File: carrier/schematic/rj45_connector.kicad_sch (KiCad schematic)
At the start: 7 parts, among them J22001 KH-5224-8P8C-D

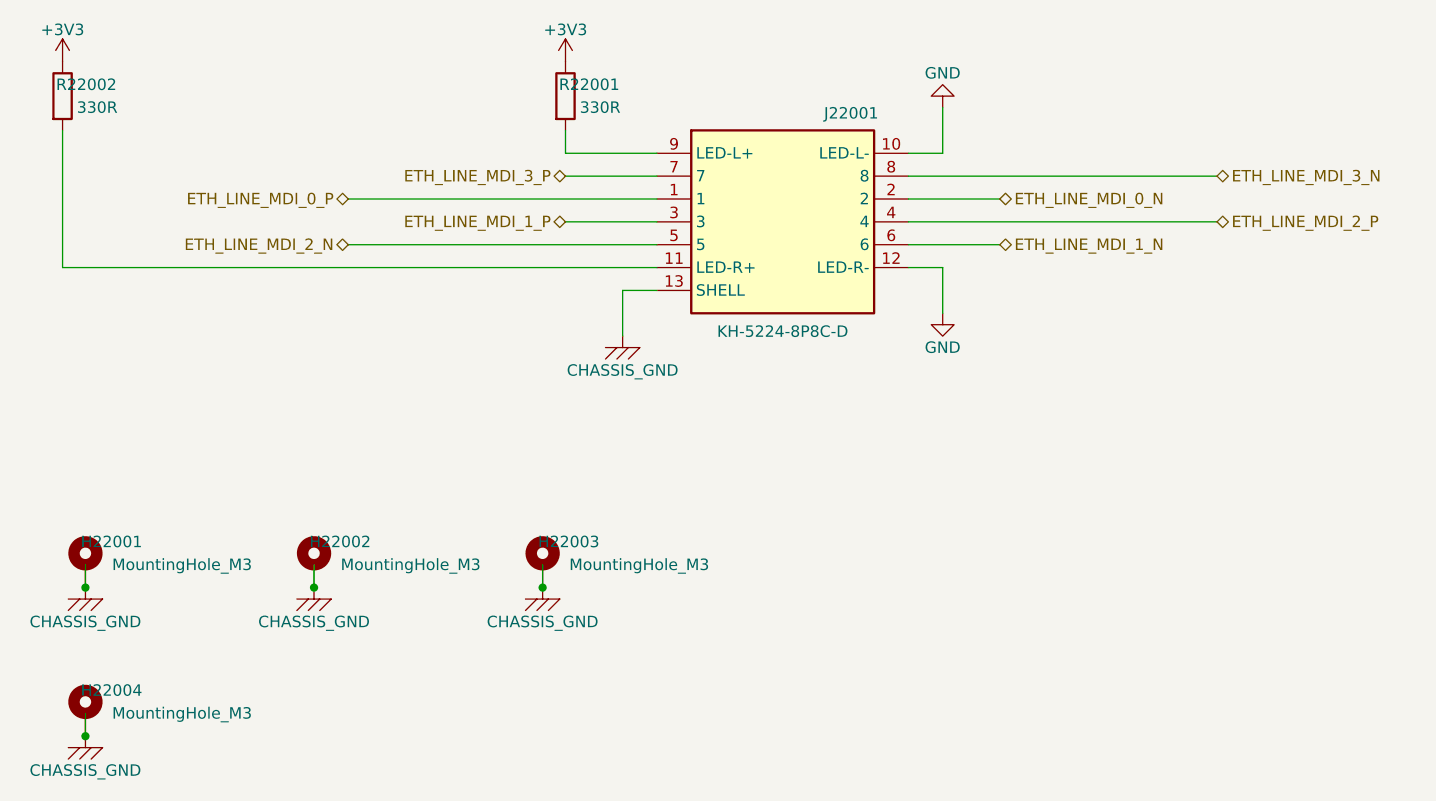
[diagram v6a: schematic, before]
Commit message: feat: USB-JTAG/UART debug bridge (CH347T) + Pmod expansion (Stream C)
Two new feature sheets (board 30 -> 33):
- usb_jtag + usb_jtag_connector: a self-powered, isolated USB-JTAG/UART debug
  bridge. CH347T (chosen over FT2232H, whose 64-pin LQFP the placer cannot route)
  on its own USB-powered island (AP2112K-3.3 LDO, USBLC6 ESD, 8MHz xtal); JTAG
  isolated to the Zynq via an SN74LVC125 buffer with default-Hi-Z OE (100k pull +
  DIP) so the existing debug_boot header owns JTAG by default (zero contention,
  netlist-proven: ZYNQ_JTAG touches only the buffer). Can program a dead board.
- pmod_expansion: a Digilent Pmod (2x6, 3.3V) — 8 IO on verified-free bank-13 PL
  pins (via FUNCTION_MAP) + a manually-gated rail + TPD4E1U06 ESD.

Pin alloc verified free (XDC 146 -> 156, no double-claims). Regression green:
board 33 sheets, selftest 59/59, pytest 219. usb_jtag render inspected (LAW 1).

Co-Authored-By: Claude Opus 4.8 <noreply@anthropic.com>
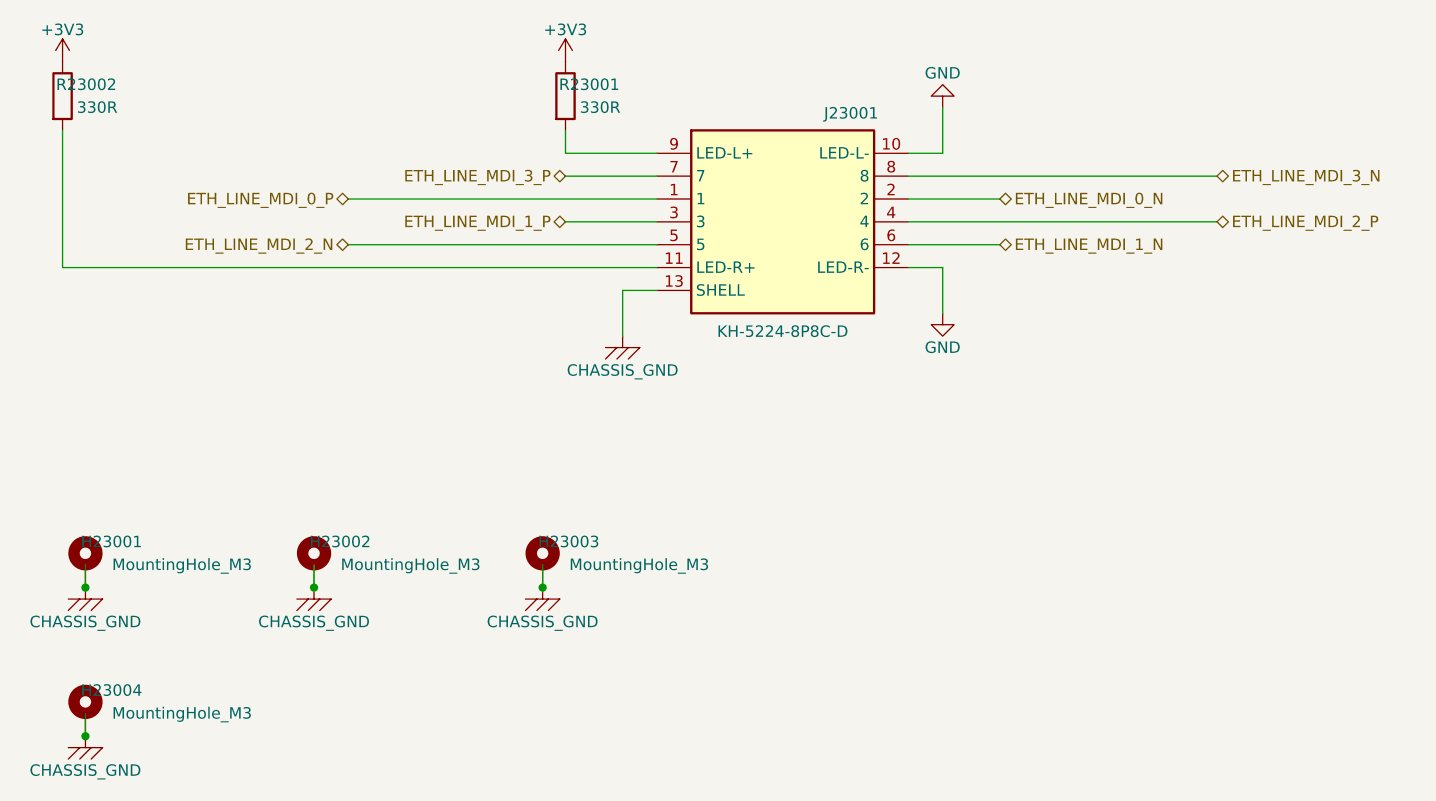
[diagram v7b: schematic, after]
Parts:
- renumbered H22001 to H23001, H22002 to H23002, H22003 to H23003, H22004 to H23004, J22001 to J23001, R22001 to R23001, R22002 to R23002
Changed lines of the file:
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@@
 		(property
 			"Reference"
-			"J22001"
+			"J23001"
 			(at 163.83 67.945 0)
 			(effects
@@
 				(path
 					"/c2797150-7a6e-556a-82f5-fdda13c31368/ae92c55a-3f4a-550a-b45e-435ced9eac9f"
-					(reference "J22001")
+					(reference "J23001")
 					(unit 1)
 				)
@@
 		(property
 			"Reference"
-			"R22001"
+			"R23001"
 			(at 134.722 64.77 0)
 			(effects
@@
 				(path
 					"/c2797150-7a6e-556a-82f5-fdda13c31368/ae92c55a-3f4a-550a-b45e-435ced9eac9f"
-					(reference "R22001")
+					(reference "R23001")
 					(unit 1)
 				)
@@
 		(property
 			"Reference"
-			"R22002"
+			"R23002"
 			(at 78.843 64.77 0)
 			(effects
@@
 				(path
 					"/c2797150-7a6e-556a-82f5-fdda13c31368/ae92c55a-3f4a-550a-b45e-435ced9eac9f"
-					(reference "R22002")
+					(reference "R23002")
 					(unit 1)
 				)
@@
 		(property
 			"Reference"
-			"H22001"
+			"H23001"
 			(at 81.637 115.57 0)
 			(effects
@@
 				(path
 					"/c2797150-7a6e-556a-82f5-fdda13c31368/ae92c55a-3f4a-550a-b45e-435ced9eac9f"
-					(reference "H22001")
+					(reference "H23001")
 					(unit 1)
 				)
@@
 		(property
 			"Reference"
-			"H22002"
+			"H23002"
 			(at 107.037 115.57 0)
 			(effects
@@
 				(path
 					"/c2797150-7a6e-556a-82f5-fdda13c31368/ae92c55a-3f4a-550a-b45e-435ced9eac9f"
-					(reference "H22002")
+					(reference "H23002")
 					(unit 1)
 				)
@@
 		(property
 			"Reference"
-			"H22003"
+			"H23003"
 			(at 132.437 115.57 0)
 			(effects
@@
 				(path
 					"/c2797150-7a6e-556a-82f5-fdda13c31368/ae92c55a-3f4a-550a-b45e-435ced9eac9f"
-					(reference "H22003")
+					(reference "H23003")
 					(unit 1)
 				)
@@
 		(property
 			"Reference"
-			"H22004"
+			"H23004"
 			(at 81.637 132.08 0)
 			(effects
@@
 				(path
 					"/c2797150-7a6e-556a-82f5-fdda13c31368/ae92c55a-3f4a-550a-b45e-435ced9eac9f"
-					(reference "H22004")
+					(reference "H23004")
 					(unit 1)
 				)
@@
 		(property
 			"Reference"
-			"#PWR22001"
+			"#PWR23001"
 			(at 138.43 90.17 0)
 			(effects
@@
 				(path
 					"/c2797150-7a6e-556a-82f5-fdda13c31368/ae92c55a-3f4a-550a-b45e-435ced9eac9f"
-					(reference "#PWR22001")
+					(reference "#PWR23001")
 					(unit 1)
 				)
@@
 		(property
 			"Reference"
-			"#PWR22002"
+			"#PWR23002"
 			(at 132.08 59.69 0)
 			(effects
@@
 				(path
 					"/c2797150-7a6e-556a-82f5-fdda13c31368/ae92c55a-3f4a-550a-b45e-435ced9eac9f"
-					(reference "#PWR22002")
+					(reference "#PWR23002")
 					(unit 1)
 				)
@@
 		(property
 			"Reference"
-			"#PWR22003"
+			"#PWR23003"
 			(at 76.2 59.69 0)
 			(effects
@@
 				(path
 					"/c2797150-7a6e-556a-82f5-fdda13c31368/ae92c55a-3f4a-550a-b45e-435ced9eac9f"
-					(reference "#PWR22003")
+					(reference "#PWR23003")
 					(unit 1)
 				)
@@
 		(property
 			"Reference"
-			"#PWR22004"
+			"#PWR23004"
 			(at 173.99 64.77 0)
 			(effects
@@
 				(path
 					"/c2797150-7a6e-556a-82f5-fdda13c31368/ae92c55a-3f4a-550a-b45e-435ced9eac9f"
-					(reference "#PWR22004")
+					(reference "#PWR23004")
 					(unit 1)
 				)
@@
 		(property
 			"Reference"
-			"#PWR22005"
+			"#PWR23005"
 			(at 173.99 87.63 0)
 			(effects
@@
 				(path
 					"/c2797150-7a6e-556a-82f5-fdda13c31368/ae92c55a-3f4a-550a-b45e-435ced9eac9f"
-					(reference "#PWR22005")
+					(reference "#PWR23005")
 					(unit 1)
 				)
@@
 		(property
 			"Reference"
-			"#PWR22009"
+			"#PWR23009"
 			(at 78.74 118.11 0)
 			(effects
@@
 				(path
 					"/c2797150-7a6e-556a-82f5-fdda13c31368/ae92c55a-3f4a-550a-b45e-435ced9eac9f"
-					(reference "#PWR22009")
+					(reference "#PWR23009")
 					(unit 1)
 				)
@@
 		(property
 			"Reference"
-			"#PWR22010"
+			"#PWR23010"
 			(at 104.14 118.11 0)
 			(effects
@@
 				(path
 					"/c2797150-7a6e-556a-82f5-fdda13c31368/ae92c55a-3f4a-550a-b45e-435ced9eac9f"
-					(reference "#PWR22010")
+					(reference "#PWR23010")
 					(unit 1)
 				)
@@
 		(property
 			"Reference"
-			"#PWR22011"
+			"#PWR23011"
 			(at 129.54 118.11 0)
 			(effects
@@
 				(path
 					"/c2797150-7a6e-556a-82f5-fdda13c31368/ae92c55a-3f4a-550a-b45e-435ced9eac9f"
-					(reference "#PWR22011")
+					(reference "#PWR23011")
 					(unit 1)
 				)
@@
 		(property
 			"Reference"
-			"#PWR22012"
+			"#PWR23012"
 			(at 78.74 134.62 0)
 			(effects
@@
 				(path
 					"/c2797150-7a6e-556a-82f5-fdda13c31368/ae92c55a-3f4a-550a-b45e-435ced9eac9f"
-					(reference "#PWR22012")
-					(unit 1)
-				)
+					(reference "#PWR23012")
+					(unit 1)
+				)

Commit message: carrier: mechanical page (mounting holes off rj45) + placer DRC root-cause fix
Extract the 4 M3 corner mounting holes (H1..H4 -> CHASSIS_GND) out of the
REUSABLE subsystems/rj45_connector library into a new carrier-LOCAL
carrier/subsystems/mechanical/ package (-> 34 sheets). They were dragged into
the ethernet jack's per-subsystem ratsnest cluster; now they are their own
corner-forced mechanical cluster. rj45 keeps J1's shell tie (the only
CHASSIS_GND item on the jack sheet). Stable refdes registry -> mechanical
appends at band 34, NO re-stride (only rj45_connector.kicad_sch changes +
mechanical.kicad_sch is new).

PLACER DRC ROOT CAUSE (the 4 U18001 intra-footprint clearance errors): the
stable-refdes commit made build_board key root-schematic refs off the frozen
carrier/sheet_index.json band, but board_parts() (the PCB pad<->net join) still
used the 1-based enumerate position. At 33 sheets the two coincide (registry
seeded alphabetically); inserting `mechanical` out of alphabetical order desynced
them, so a later sheet's refs disagreed (U18001 vs U17001) and the pad<->net join
silently missed -> pmod's pads (incl a thermal-pad EP) landed no-net -> no-net EP
copper clashed with its no-net thermal vias -> intra-footprint clearance DRC.
Fix: board_parts() reads the same sheet_index.json band. (LAW 4: no DRC waiver.)

Also: pcb.py excludes corner-forced mounting holes from zone-packing (so STEP 3's
corner-force is not overwritten), and the LAW-5 ratsnest gate excludes
MountingHole footprints from the per-subsystem DISPERSION metric (corner-spread
fab-art is not a free-placement scatter — same rationale that skips the fixed SoM
receptacle sheets) while still enforcing they stay ON-BOARD.

Verify: BOARD PASS (34 sheets), PCB DRC 0, RATSNEST LAW-5 PASS (0 off-board,
0 dispersed), CARRIER STRUCTURE 34/34, CC 0/0, selftest determinism+hash-seed
PASS, golden blessed 34 (only rj45+mechanical renders changed), 33 subsystem
tests pass.

Co-Authored-By: Claude Opus 4.8 <noreply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
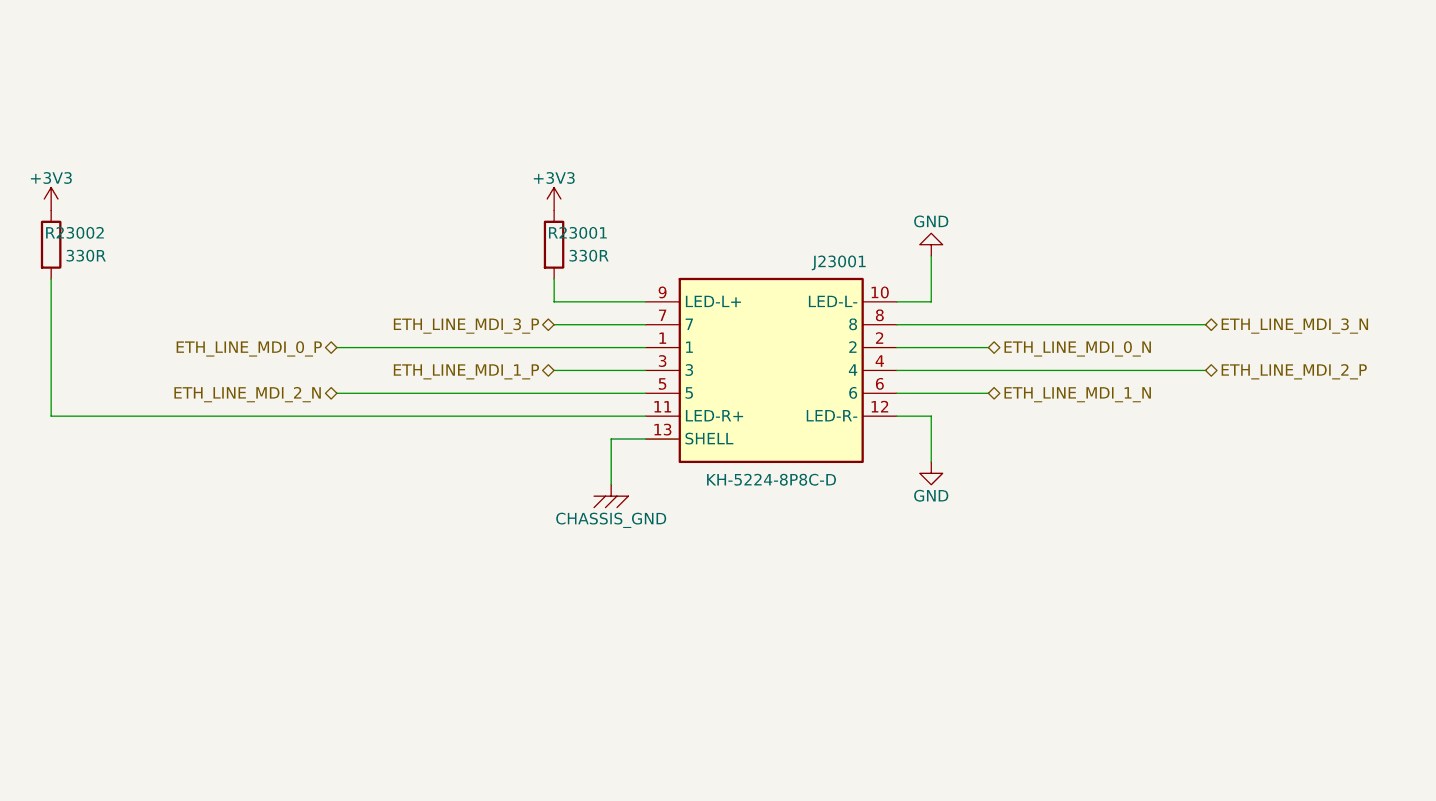
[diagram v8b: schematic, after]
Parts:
- removed H23001, H23002, H23003, H23004: MountingHole_M3, MountingHole:MountingHole_3.2mm_M3_Pad, symbol Mechanical:MountingHole_Pad
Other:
- moved on the sheet: J23001, R23001, R23002
